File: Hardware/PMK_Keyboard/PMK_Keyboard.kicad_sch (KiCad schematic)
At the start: 110 parts, among them IC1 SN74HC165PWR, IC10 SN74HC165PWR, IC2 SN74HC165PWR, IC20 SN74HC165PWR, IC30 SN74HC165PWR, IC40 SN74HC165PWR, IC50 SN74HC165PWR, IC60 SN74HC165PWR, IC70 SN74HC165PWR, IC80 SN74HC165PWR, IC90 SN74HC165PWR, SW1 SW_Push, SW10 SW_Push, SW11 SW_Push, SW12 SW_Push, SW13 SW_Push, SW14 SW_Push, SW15 SW_Push, SW16 SW_Push, SW17 SW_Push, SW18 SW_Push, SW19 SW_Push, SW2 SW_Push, SW20 SW_Push, SW21 SW_Push, SW22 SW_Push, SW23 SW_Push, SW24 SW_Push, SW25 SW_Push, SW26 SW_Push, SW27 SW_Push, SW28 SW_Push, SW29 SW_Push, SW3 SW_Push, SW30 SW_Push, SW31 SW_Push, SW32 SW_Push, SW33 SW_Push, SW34 SW_Push, SW35 SW_Push, SW36 SW_Push, SW37 SW_Push, SW38 SW_Push, SW39 SW_Push, SW4 SW_Push, SW40 SW_Push, SW41 SW_Push, SW42 SW_Push, SW43 SW_Push, SW44 SW_Push, SW45 SW_Push, SW46 SW_Push, SW47 SW_Push, SW48 SW_Push, SW49 SW_Push, SW5 SW_Push, SW50 SW_Push, SW51 SW_Push, SW52 SW_Push, SW53 SW_Push, SW54 SW_Push, SW55 SW_Push, SW56 SW_Push, SW57 SW_Push, SW58 SW_Push, SW59 SW_Push, SW6 SW_Push, SW60 SW_Push, SW61 SW_Push, SW62 SW_Push, SW63 SW_Push, SW64 SW_Push, SW65 SW_Push, SW66 SW_Push, SW67 SW_Push, SW68 SW_Push, SW69 SW_Push, SW7 SW_Push, SW70 SW_Push, SW71 SW_Push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

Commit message: project update
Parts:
- removed IC2, IC60, IC70, IC80, IC90: SN74HC165PWR, SOP65P640X120-16N, symbol Component_lib:SN74HC165PWR
- removed RN100, RN60, RN70, RN80, RN90: R_Network08, Resistor_THT:R_Array_SIP9, symbol Device:R_Network08
- removed SW49, SW50, SW51, SW52, SW53, SW54, SW55, SW56, SW57, SW58, SW59, SW60, SW61, SW62, SW63, SW64, SW65, SW66, SW67, SW68, SW69, SW70, SW71, SW72, SW73, SW74, SW75, SW76, SW77, SW78, SW79, SW80, SW81, SW82, SW83, SW84, SW85, SW86, SW87, SW88: SW_Push, symbol Switch:SW_Push
- IC1: footprint SOP65P640X120-16N -> Component_lib:SOP65P640X120-16N
- IC2: renamed from IC10; footprint SOP65P640X120-16N -> Component_lib:SOP65P640X120-16N
- IC3: renamed from IC20; footprint SOP65P640X120-16N -> Component_lib:SOP65P640X120-16N
- IC4: renamed from IC30; footprint SOP65P640X120-16N -> Component_lib:SOP65P640X120-16N
- IC5: renamed from IC40; footprint SOP65P640X120-16N -> Component_lib:SOP65P640X120-16N
- IC6: renamed from IC50; footprint SOP65P640X120-16N -> Component_lib:SOP65P640X120-16N
- RN1: footprint Resistor_THT:R_Array_SIP9 -> Resistor_SMD:R_Array_Convex_8x0602
- RN2: renamed from RN10; footprint Resistor_THT:R_Array_SIP9 -> Component_lib:Kailh_socket_PG1350_optional_reversible
- RN3: renamed from RN20; footprint Resistor_THT:R_Array_SIP9 -> Component_lib:Kailh_socket_PG1350_optional_reversible
- RN4: renamed from RN30; footprint Resistor_THT:R_Array_SIP9 -> Component_lib:Kailh_socket_PG1350_optional_reversible
- RN5: renamed from RN40; footprint Resistor_THT:R_Array_SIP9 -> Component_lib:Kailh_socket_PG1350_optional_reversible
- RN6: renamed from RN50; footprint Resistor_THT:R_Array_SIP9 -> Component_lib:Kailh_socket_PG1350_optional_reversible
- SW1, SW2, SW33, SW34, SW35, SW36, SW37, SW38, SW39, SW40, SW41, SW42, SW43, SW44, SW45, SW46, SW47, SW48: footprint (none) -> Component_lib:Kailh_socket_PG1350_optional_reversible
- SW10: renamed from SW18; footprint (none) -> Component_lib:Kailh_socket_PG1350_optional_reversible
- SW11: renamed from SW19; footprint (none) -> Component_lib:Kailh_socket_PG1350_optional_reversible
- SW12: renamed from SW20; footprint (none) -> Component_lib:Kailh_socket_PG1350_optional_reversible
- SW13: renamed from SW21; footprint (none) -> Component_lib:Kailh_socket_PG1350_optional_reversible
- SW14: renamed from SW22; footprint (none) -> Component_lib:Kailh_socket_PG1350_optional_reversible
- SW15: renamed from SW23; footprint (none) -> Component_lib:Kailh_socket_PG1350_optional_reversible
- SW16: renamed from SW24; footprint (none) -> Component_lib:Kailh_socket_PG1350_optional_reversible
- SW17: renamed from SW25; footprint (none) -> Component_lib:Kailh_socket_PG1350_optional_reversible
- SW18: renamed from SW26; footprint (none) -> Component_lib:Kailh_socket_PG1350_optional_reversible
- SW19: renamed from SW27; footprint (none) -> Component_lib:Kailh_socket_PG1350_optional_reversible
- SW20: renamed from SW28; footprint (none) -> Component_lib:Kailh_socket_PG1350_optional_reversible
- SW21: renamed from SW29; footprint (none) -> Component_lib:Kailh_socket_PG1350_optional_reversible
- SW22: renamed from SW30; footprint (none) -> Component_lib:Kailh_socket_PG1350_optional_reversible
- SW23: renamed from SW31; footprint (none) -> Component_lib:Kailh_socket_PG1350_optional_reversible
- SW24: renamed from SW32; footprint (none) -> Component_lib:Kailh_socket_PG1350_optional_reversible
- SW25: renamed from SW3; footprint (none) -> Component_lib:Kailh_socket_PG1350_optional_reversible
- SW26: renamed from SW4; footprint (none) -> Component_lib:Kailh_socket_PG1350_optional_reversible
- SW27: renamed from SW5; footprint (none) -> Component_lib:Kailh_socket_PG1350_optional_reversible
- SW28: renamed from SW6; footprint (none) -> Component_lib:Kailh_socket_PG1350_optional_reversible
- SW29: renamed from SW7; footprint (none) -> Component_lib:Kailh_socket_PG1350_optional_reversible
- SW3: renamed from SW11; footprint (none) -> Component_lib:Kailh_socket_PG1350_optional_reversible
- SW30: renamed from SW8; footprint (none) -> Component_lib:Kailh_socket_PG1350_optional_reversible
- SW31: renamed from SW9; footprint (none) -> Component_lib:Kailh_socket_PG1350_optional_reversible
- SW32: renamed from SW10; footprint (none) -> Component_lib:Kailh_socket_PG1350_optional_reversible
- SW4: renamed from SW12; footprint (none) -> Component_lib:Kailh_socket_PG1350_optional_reversible
- SW5: renamed from SW13; footprint (none) -> Component_lib:Kailh_socket_PG1350_optional_reversible
- SW6: renamed from SW14; footprint (none) -> Component_lib:Kailh_socket_PG1350_optional_reversible
- SW7: renamed from SW15; footprint (none) -> Component_lib:Kailh_socket_PG1350_optional_reversible
- SW8: renamed from SW16; footprint (none) -> Component_lib:Kailh_socket_PG1350_optional_reversible
- SW9: renamed from SW17; footprint (none) -> Component_lib:Kailh_socket_PG1350_optional_reversible

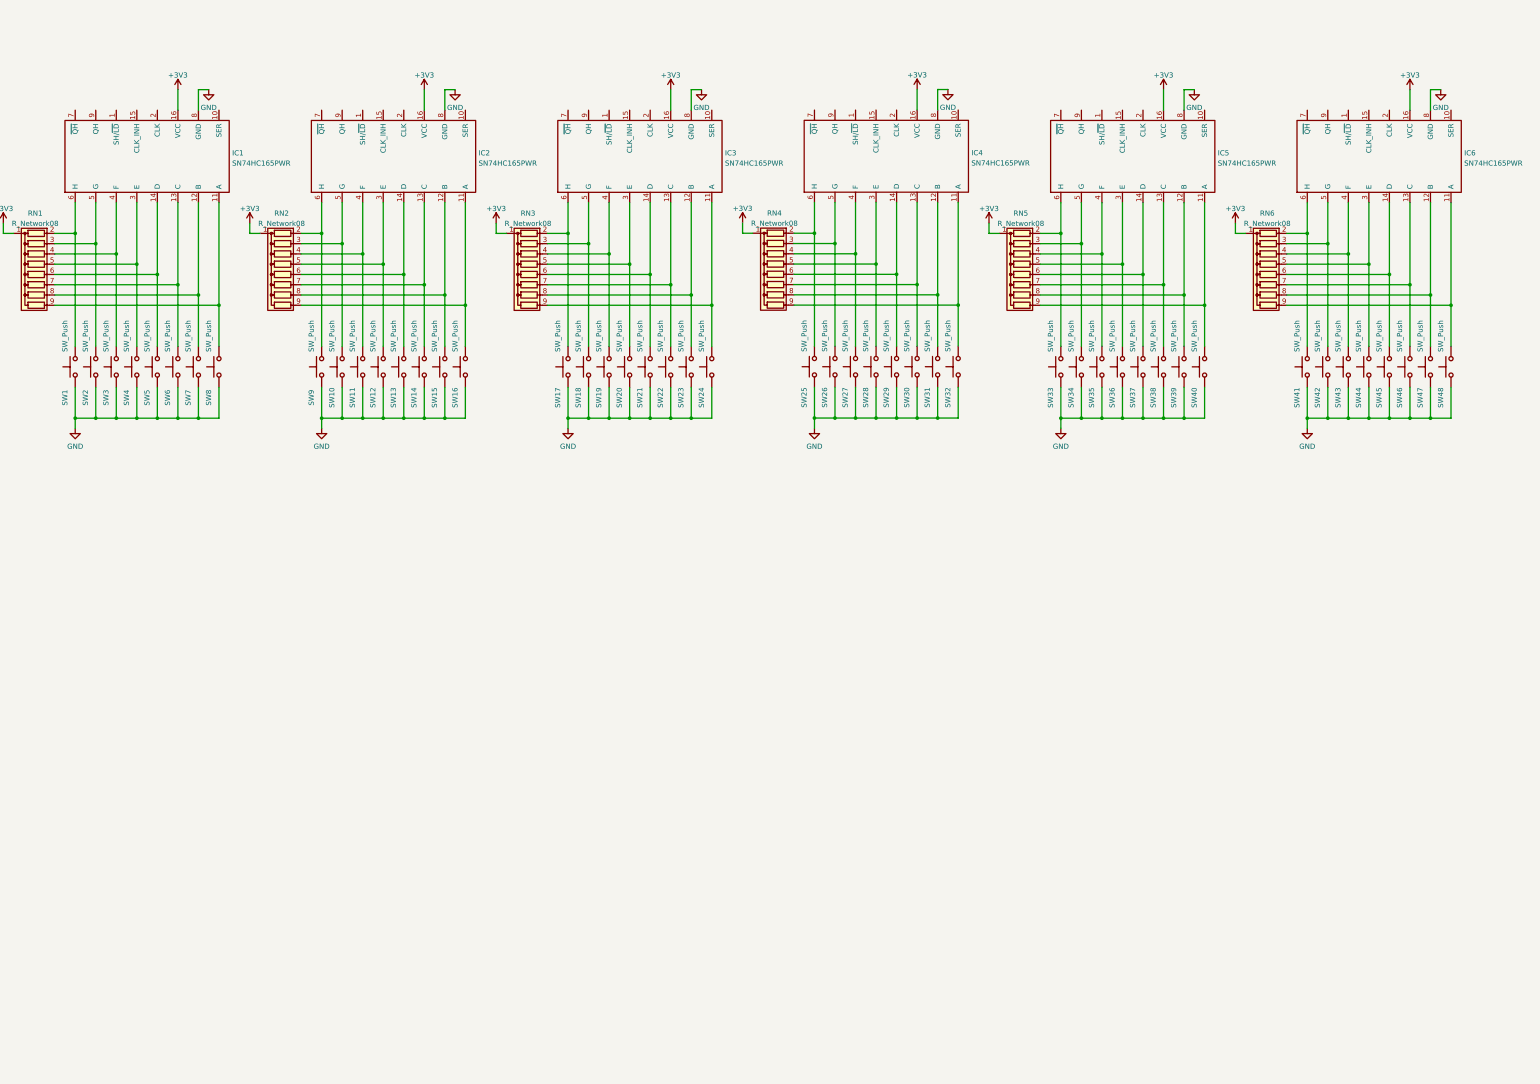
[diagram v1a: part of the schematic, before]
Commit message: Initiated layout
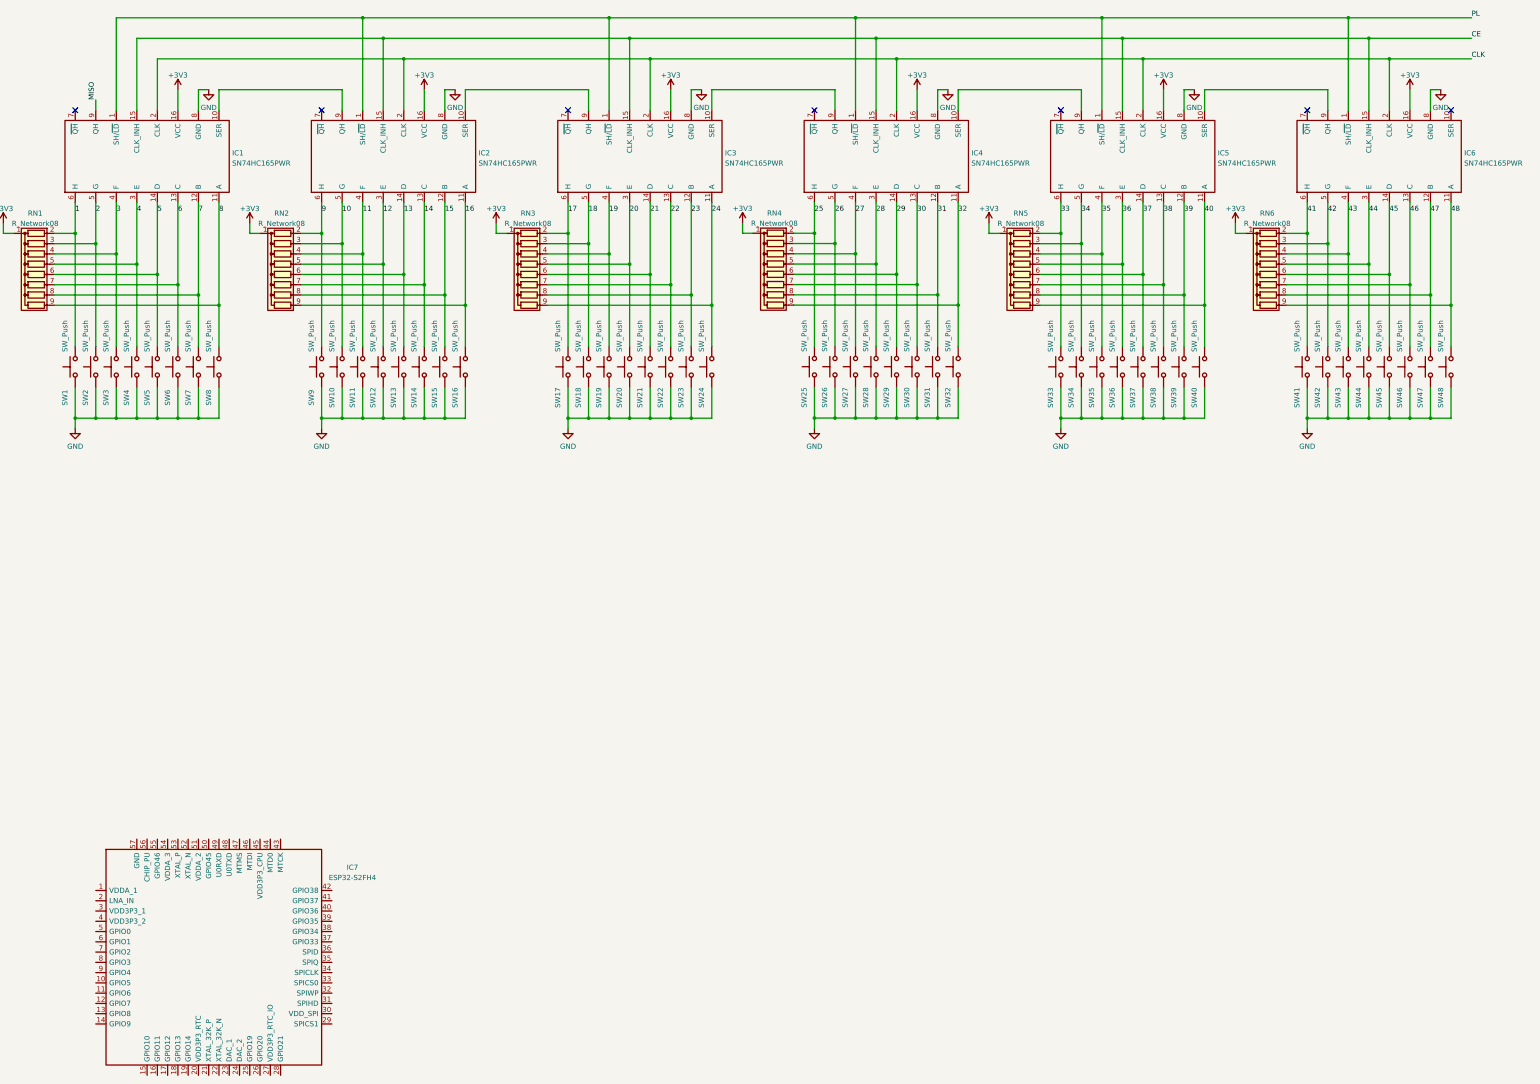
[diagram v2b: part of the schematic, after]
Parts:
- added IC7: ESP32-S2FH4, QFN40P700X700X90-57N-D, symbol Component lib:ESP32-S2FH4
- RN2, RN3, RN4, RN5, RN6: footprint Component_lib:Kailh_socket_PG1350_optional_reversible -> Resistor_SMD:R_Array_Convex_8x0602
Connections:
- net 9: now reaches IC2.6 (H), RN2.2 (R1), SW9.2
- net 13: now reaches IC2.14 (D), RN2.6 (R5), SW13.2
- net 16: now reaches IC2.11 (A), RN2.9 (R8), SW16.2
- net 10: now reaches IC2.5 (G), RN2.3 (R2), SW10.2
- net 11: now reaches IC2.4 (F), RN2.4 (R3), SW11.2
- net 12: now reaches IC2.3 (E), RN2.5 (R4), SW12.2
- net 14: now reaches IC2.13 (C), RN2.7 (R6), SW14.2
- net 15: now reaches IC2.12 (B), RN2.8 (R7), SW15.2
- net PL: now reaches IC4.1 (SH/~{LD})
- net PL: now also IC1.1 (SH/~{LD}), IC2.1 (SH/~{LD}), IC3.1 (SH/~{LD}), IC5.1 (SH/~{LD}), IC6.1 (SH/~{LD})
- net at IC4.10 (SER): now also IC5.9 (QH)
- net 32: now reaches IC4.11 (A), RN4.9 (R8), SW32.2
- net 31: now reaches IC4.12 (B), RN4.8 (R7), SW31.2
- net 30: now reaches IC4.13 (C), RN4.7 (R6), SW30.2
- net 29: now reaches IC4.14 (D), RN4.6 (R5), SW29.2
- net CE: now reaches IC4.15 (CLK_INH)
- net CE: now also IC1.15 (CLK_INH), IC2.15 (CLK_INH), IC3.15 (CLK_INH), IC5.15 (CLK_INH), IC6.15 (CLK_INH)
- net CLK: now reaches IC4.2 (CLK)
- net CLK: now also IC1.2 (CLK), IC2.2 (CLK), IC3.2 (CLK), IC5.2 (CLK), IC6.2 (CLK)
- net 28: now reaches IC4.3 (E), RN4.5 (R4), SW28.2
- net 27: now reaches IC4.4 (F), RN4.4 (R3), SW27.2
- net 26: now reaches IC4.5 (G), RN4.3 (R2), SW26.2
- net 25: now reaches IC4.6 (H), RN4.2 (R1), SW25.2
- net at IC4.9 (QH): now also IC3.10 (SER)
- net at IC2.10 (SER): now also IC3.9 (QH)
- net at IC2.9 (QH): now also IC1.10 (SER)
- net 42: now reaches IC6.5 (G), RN6.3 (R2), SW42.2
- net 5: now reaches IC1.14 (D), RN1.6 (R5), SW5.2
- net 33: now reaches IC5.6 (H), RN5.2 (R1), SW33.2
- net 36: now reaches IC5.3 (E), RN5.5 (R4), SW36.2
- net 41: now reaches IC6.6 (H), RN6.2 (R1), SW41.2
- net 40: now reaches IC5.11 (A), RN5.9 (R8), SW40.2
- net 34: now reaches IC5.5 (G), RN5.3 (R2), SW34.2
- net 35: now reaches IC5.4 (F), RN5.4 (R3), SW35.2
- net 37: now reaches IC5.14 (D), RN5.6 (R5), SW37.2
- net 38: now reaches IC5.13 (C), RN5.7 (R6), SW38.2
- net 39: now reaches IC5.12 (B), RN5.8 (R7), SW39.2
- net 23: now reaches IC3.12 (B), RN3.8 (R7), SW23.2
- net 20: now reaches IC3.3 (E), RN3.5 (R4), SW20.2
- net 17: now reaches IC3.6 (H), RN3.2 (R1), SW17.2
- net 1: now reaches IC1.6 (H), RN1.2 (R1), SW1.2
- net 2: now reaches IC1.5 (G), RN1.3 (R2), SW2.2
- net 3: now reaches IC1.4 (F), RN1.4 (R3), SW3.2
- net 4: now reaches IC1.3 (E), RN1.5 (R4), SW4.2
- net 6: now reaches IC1.13 (C), RN1.7 (R6), SW6.2
- net 7: now reaches IC1.12 (B), RN1.8 (R7), SW7.2
- net 8: now reaches IC1.11 (A), RN1.9 (R8), SW8.2
- net 48: now reaches IC6.11 (A), RN6.9 (R8), SW48.2
- net 47: now reaches IC6.12 (B), RN6.8 (R7), SW47.2
- net 46: now reaches IC6.13 (C), RN6.7 (R6), SW46.2
- net 45: now reaches IC6.14 (D), RN6.6 (R5), SW45.2
- net 44: now reaches IC6.3 (E), RN6.5 (R4), SW44.2
- net 43: now reaches IC6.4 (F), RN6.4 (R3), SW43.2
- net at IC6.9 (QH): now also IC5.10 (SER)
- net 18: now reaches IC3.5 (G), RN3.3 (R2), SW18.2
- net 19: now reaches IC3.4 (F), RN3.4 (R3), SW19.2
- net 21: now reaches IC3.14 (D), RN3.6 (R5), SW21.2
- net 22: now reaches IC3.13 (C), RN3.7 (R6), SW22.2
- net 24: now reaches IC3.11 (A), RN3.9 (R8), SW24.2
- net MISO: now reaches IC1.9 (QH)
- no-connect marks 0 -> 7
